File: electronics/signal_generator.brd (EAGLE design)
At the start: 50.8 x 28.9 mm, 8 parts, among them IC1 LM386N-1

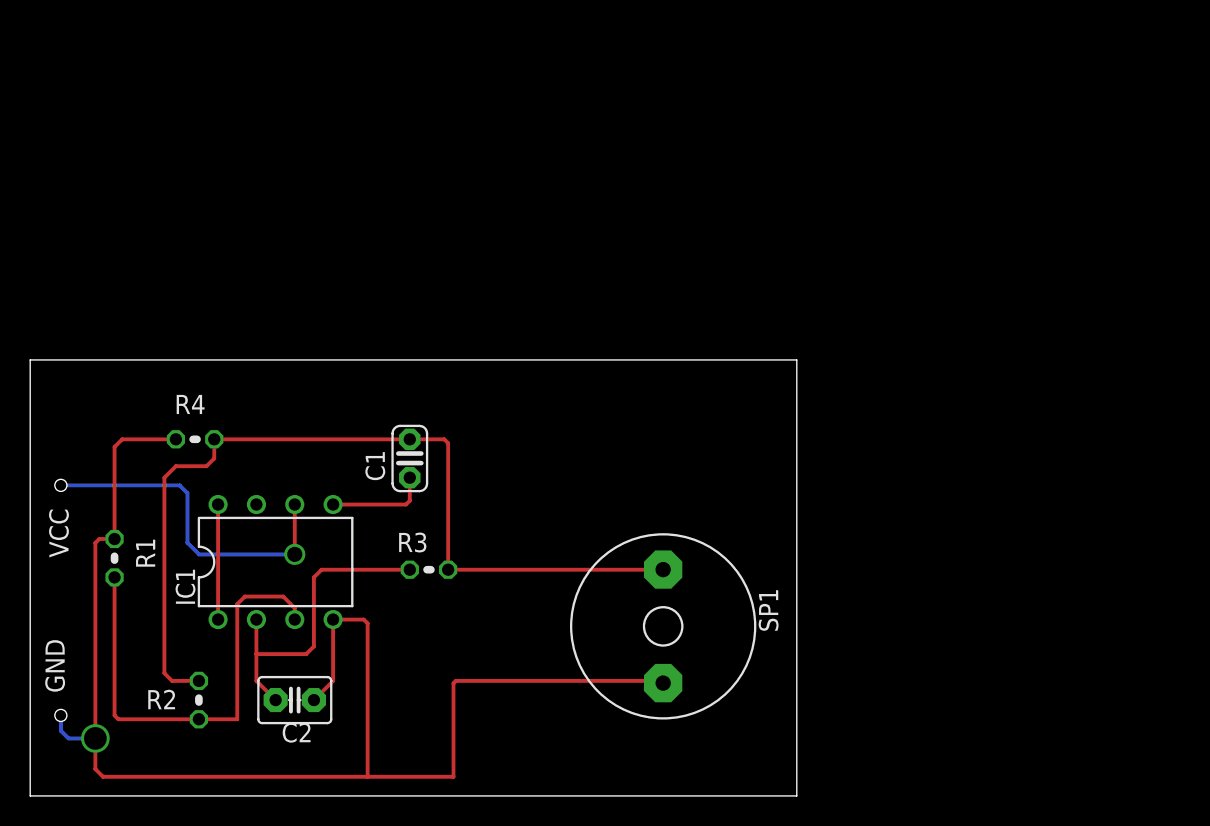
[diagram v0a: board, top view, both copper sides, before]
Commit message: increase size of routes and pads
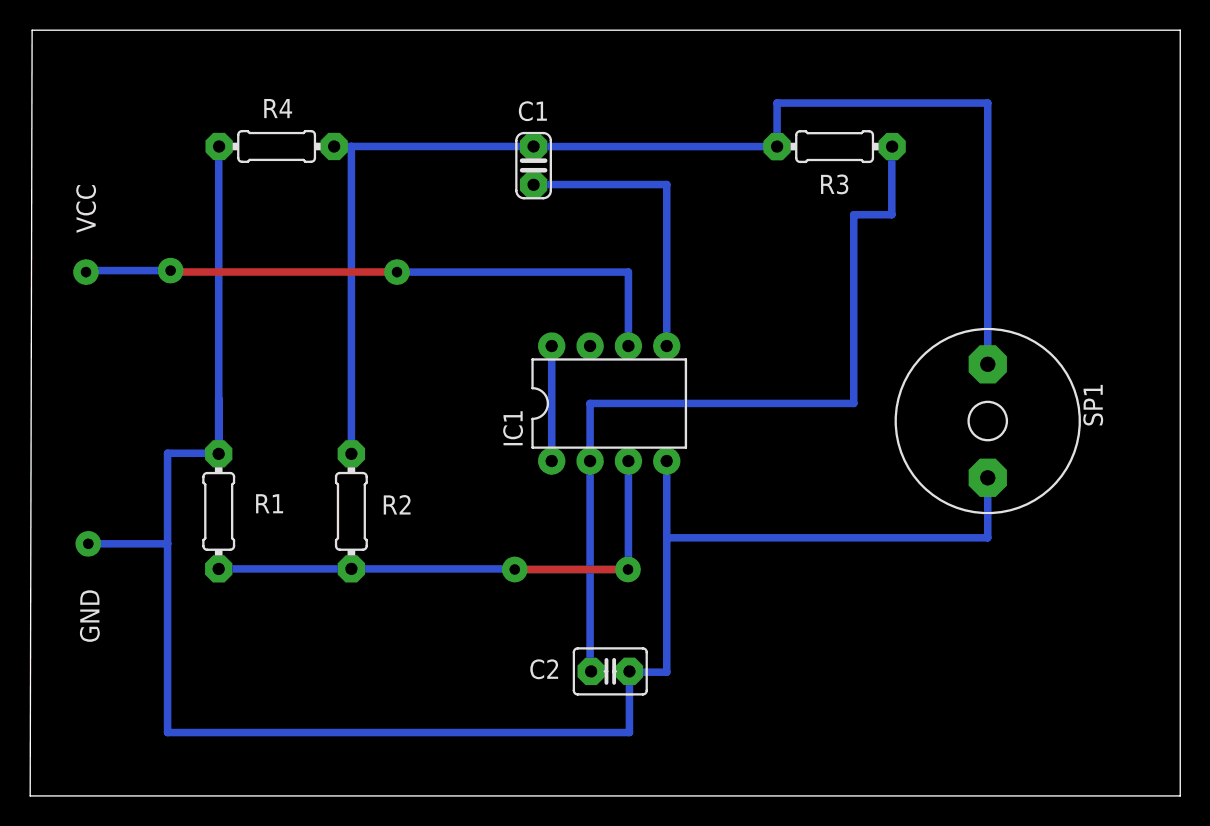
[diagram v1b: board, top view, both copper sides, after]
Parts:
- R1, R2, R3, R4: device adafruit:0204V -> adafruit:0204/7
- moved R3 38.8 mm to (53.3, 43.0), turned to 180 degrees
- moved SP1 25.4 mm to (63.4, 24.8)
- moved IC1 24.5 mm to (38.4, 26.0)
- moved C1 21.1 mm to (33.3, 41.8)
- moved C2 21.0 mm to (38.4, 8.25)
- moved R4 20.1 mm to (16.3, 43.0)
- moved R2 16.1 mm to (21.3, 18.9)
- moved R1 7.56 mm to (12.5, 18.8)
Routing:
- net GND: track 92.8 -> 127.6 mm
- net PIN2: track 21.0 -> 54.8 mm
- net OUT: track 58.8 -> 83.9 mm
- net VCC: track 22.6 -> 41.0 mm, vias 1 -> 3
- net PIN5: track 6.71 -> 19.5 mm
- net PIN3: track 30.1 -> 34.3 mm, vias 0 -> 2
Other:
- board size 50.8 x 28.9 mm -> 76.2 x 50.7 mm
